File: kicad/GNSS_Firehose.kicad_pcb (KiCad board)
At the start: 4 copper layers, 117.9 x 99.1 mm, 460 parts, among them J1 SMA, J10 HEADER_16, J2 SMA, J3 SMA, J4 SMA, J5 SMA, J6 HEADER_14, J7 L829-1J1T-43, J8 PJ-063BH, Q1 Si2369DS, U1 MAX2112, U10 MAX19505, U11 AT25DF041A, U12 XC6SLX9-2TQG144C, U15 LMK03806, U17 LTC3633, U18 KSZ9031RNX, U19 CDCLVC1102, U2 MAX19505, U20 MIC2090-1YM5, U21 MIC2090-1YM5, U22 MIC2090-1YM5, U3 MGA-68563, U4 MAX2112, U5 MAX19505, U6 MGA-68563, U7 MAX2112, U8 MAX19505, U9 MGA-68563, Y1 25 MHz

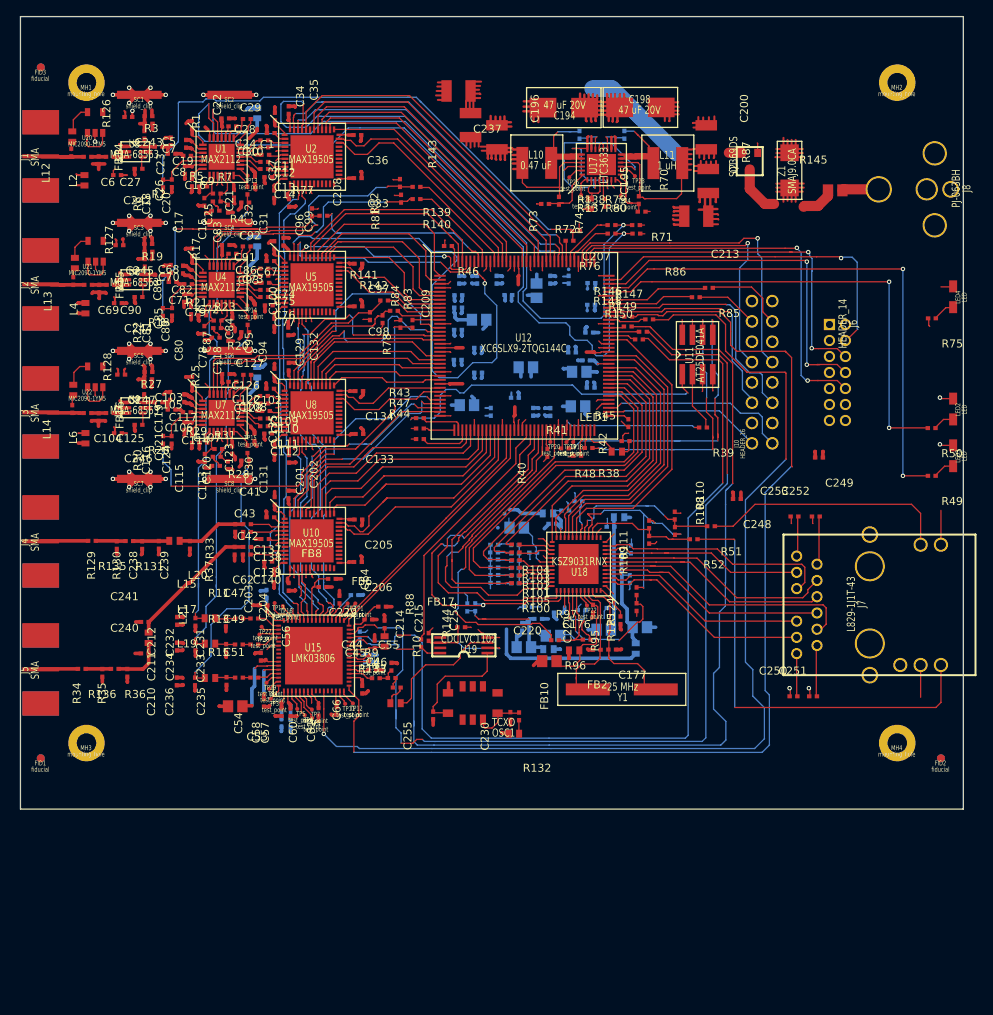
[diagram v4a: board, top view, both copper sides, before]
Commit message: add power-plane cutouts
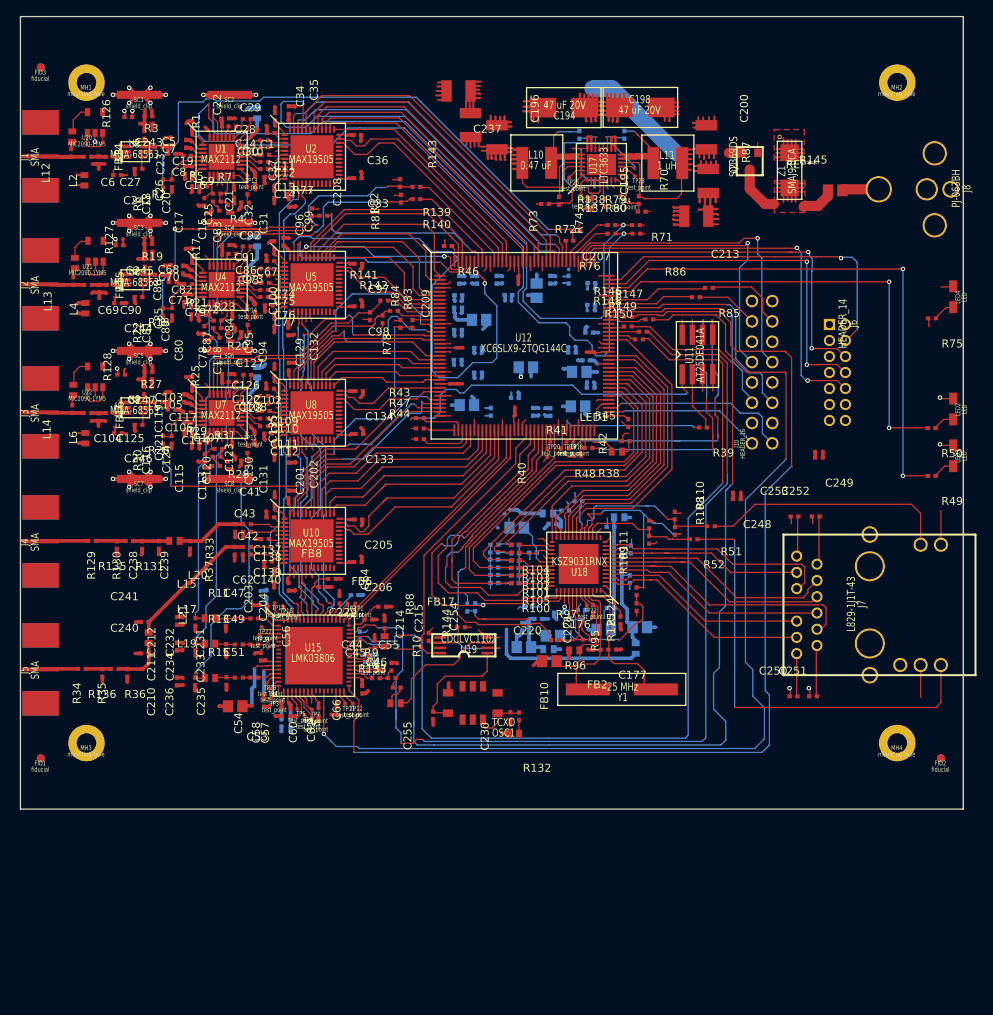
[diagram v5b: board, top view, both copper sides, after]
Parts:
- added REF**: via_12mil, footprints:via_12mil, F.Cu at (168.6, 58.2)
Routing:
- net VCC_1.2V: vias 0 -> 1
- net /RF channel 1/ch1_vcc_lna: vias 0 -> 1
- net /RF channel 1/ch1_vcc: vias 0 -> 1
- net /RF Channel 3/ch3_vcc_lna: vias 0 -> 1
- net /RF Channel 3/ch3_vcc: vias 0 -> 1
- net /RF Channel 2/ch2_vcc_lna: vias 0 -> 1
- net /RF Channel 2/ch2_vcc: vias 0 -> 1
- net /Ethernet/DVDDL: vias 0 -> 1
- net /Ethernet/DVDDH: vias 0 -> 1
- added copper zone on In2.Cu, net /Ethernet/DVDDH
- added copper zone on In2.Cu, net /Ethernet/DVDDL
- added copper zone on In2.Cu, net /RF Channel 2/ch2_vcc
- added copper zone on In2.Cu, net /RF Channel 2/ch2_vcc_lna
- added copper zone on In2.Cu, net /RF Channel 3/ch3_vcc
- added copper zone on In2.Cu, net /RF Channel 3/ch3_vcc_lna
- added copper zone on In2.Cu, net /RF channel 1/ch1_vcc
- added copper zone on In2.Cu, net /RF channel 1/ch1_vcc_lna
- added copper zone on F.Cu, net GND
- added copper zone on F.Cu, net Net-(Q1-Pad3)
- added copper zone on In2.Cu, net VCC_1.2V

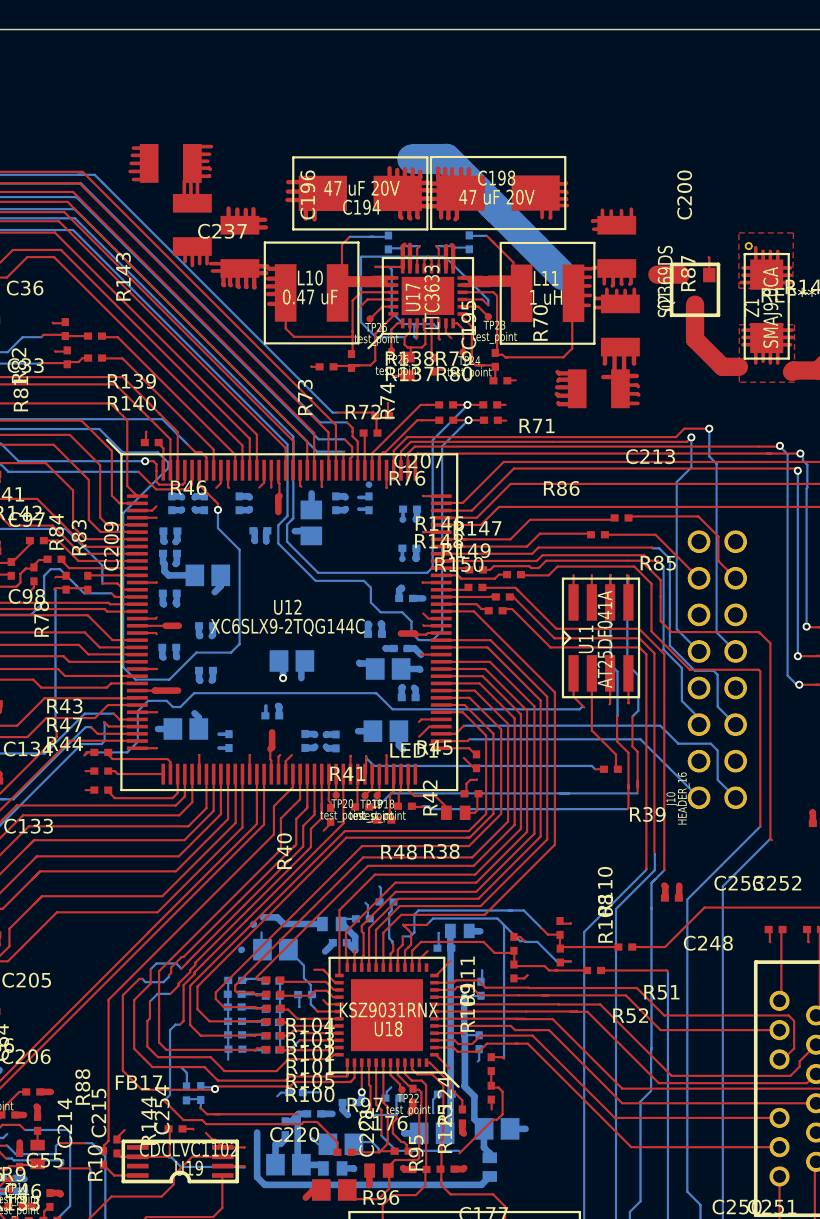
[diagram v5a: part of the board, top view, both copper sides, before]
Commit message: add small polygons
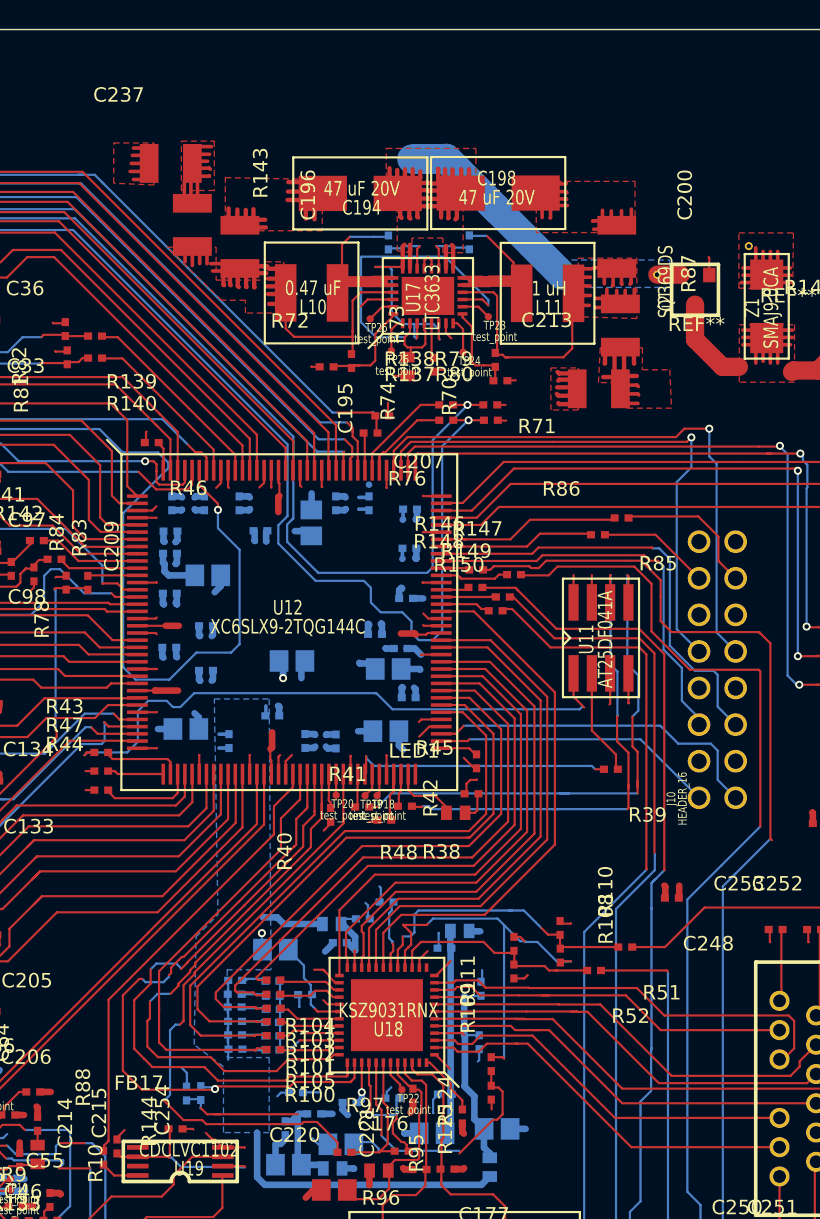
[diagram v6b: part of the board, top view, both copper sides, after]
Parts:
- added REF**: via_12mil, footprints:via_12mil, F.Cu at (162.2, 60.2)
- turned C182 to 180 degrees
- turned C183 to 180 degrees
- turned C193 to 180 degrees
- turned C195 to 270 degrees
- turned C197 to 270 degrees
- turned C213 to 180 degrees
- turned C223 to 180 degrees
- turned C237 to 180 degrees
- turned L10 to 180 degrees
- turned L11 to 180 degrees
- turned R143 to 90 degrees
- turned R70 to 270 degrees
- turned R72 to 180 degrees
- turned R73 to 90 degrees
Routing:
- net Net-(C199-Pad2): track 16.0 -> 25.1 mm
- net GND: track 430.9 -> 422.6 mm, vias 38 -> 39
- net Net-(C200-Pad1): track 30.9 -> 25.7 mm
- net (no net): track 1393.3 -> 1388.6 mm
- net Net-(R72-Pad1): track 4.64 -> 7.46 mm
- net /Ethernet/DVDDL: track 20.2 -> 22.9 mm
- net VCC_3.3V: track 161.6 -> 164.4 mm
- net /Ethernet/DVDDH: track 33.7 -> 36.0 mm
- net Net-(R70-Pad2): track 8.70 -> 6.44 mm
- net Net-(C197-Pad1): track 17.2 -> 15.1 mm
- net Net-(C197-Pad2): track 2.94 -> 3.81 mm
- added copper zone on B.Cu, net Net-(C194-Pad1)
- added copper zone on F.Cu, net Net-(C194-Pad1)
- added copper zone on F.Cu, net Net-(C196-Pad1)
- added copper zone on F.Cu, net Net-(C200-Pad1)
- added copper zone on B.Cu, net VCC_1.2V
- added copper zone on F.Cu, net VCC_1.2V
- added copper zone on F.Cu, net VCC_3.3V
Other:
- net class Default: clearance 0.15 -> 0.14986
- net class wide: clearance 0.15 -> 0.14986
- rule trace_clearance: 0.15 -> 0.14986

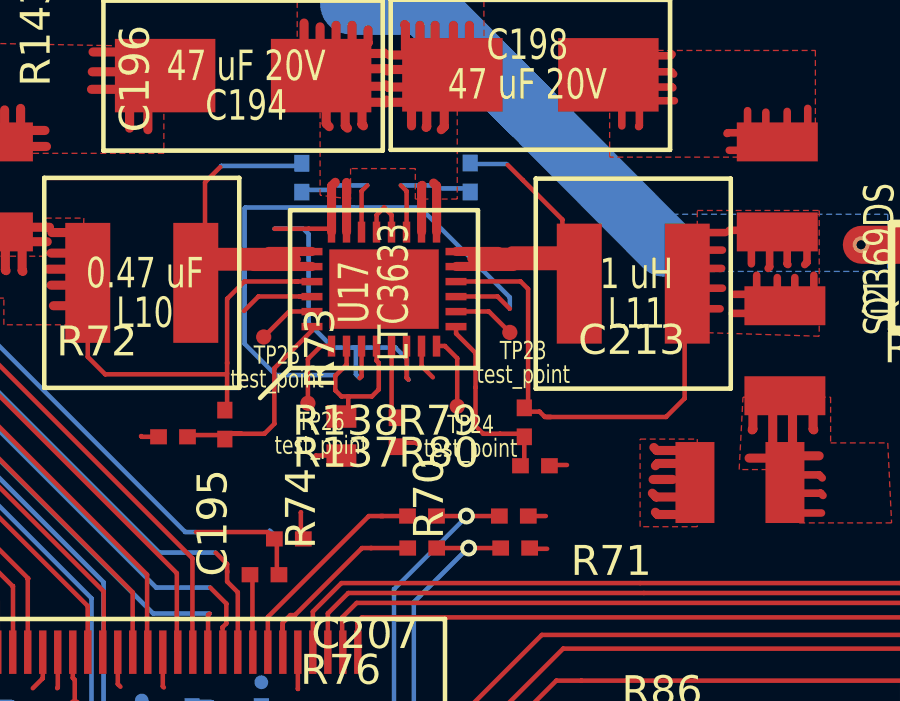
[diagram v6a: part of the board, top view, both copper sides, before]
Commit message: fix nearly all DRC errors
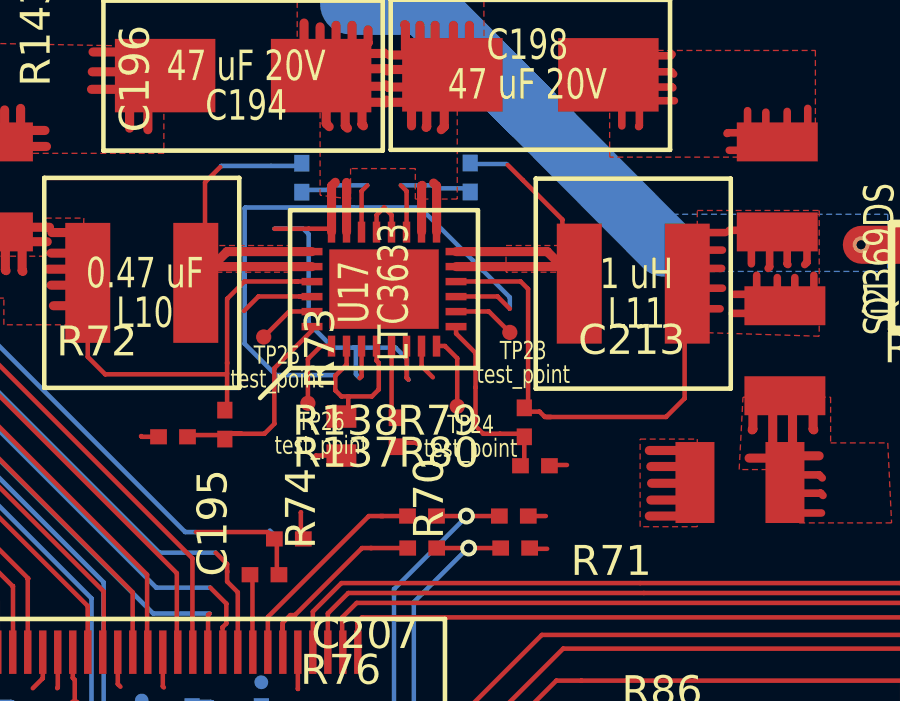
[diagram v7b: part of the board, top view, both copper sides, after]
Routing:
- net Net-(C199-Pad2): track 25.1 -> 16.2 mm
- net GND: track 422.6 -> 429.6 mm
- net (no net): track 1388.6 -> 1385.3 mm
- added copper zone on F.Cu, net Net-(C197-Pad1)
- added copper zone on F.Cu, net Net-(C199-Pad2)

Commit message: place vias
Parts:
- added G***: LOGO, footprints:diff-top, F.Cu at (132.6, 92.7)
- moved R126 0.21 mm to (80.3, 58.0)
- moved J2 0.06 mm to (73.2, 76.7)
- moved J3 0.06 mm to (73.2, 92.7)
- moved J4 0.06 mm to (73.1, 108.7)
- moved J1 0.06 mm to (73.2, 60.7)
- moved J5 0.06 mm to (73.2, 124.7)
- moved U21 0.06 mm to (82.1, 73.9)
- moved OSC1 0.06 mm to (134.0, 131.7)
- moved L12 0.05 mm to (80.0, 60.2)
- turned C53 to 180 degrees
- turned FB7 to 180 degrees
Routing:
- net (no net): track 1385.3 -> 200.2 mm
- net CLOCK_LE: track 32.6 -> 124.5 mm, vias 0 -> 3
- net CLOCK_DATA: track 29.9 -> 120.6 mm, vias 0 -> 3
- net CLOCK_FTEST_LD: track 47.4 -> 136.3 mm, vias 0 -> 1
- net CLOCK_CLK: track 28.7 -> 114.8 mm, vias 0 -> 3
- net CH1_GC1_FPGA_LPF: track 4.76 -> 71.0 mm, vias 0 -> 1
- net CH1_CLK+: track 3.72 -> 58.5 mm, vias 0 -> 2
- net CH1_REF+: track 3.99 -> 57.9 mm, vias 0 -> 2
- net CH1_CLK-: track 5.01 -> 58.6 mm, vias 0 -> 2
- net CH3_GC1_FPGA_LPF: track 3.01 -> 51.2 mm, vias 0 -> 4
- net CH1_SDIN: track 4.60 -> 52.1 mm, vias 0 -> 1
- net CH2_REF+: track 3.80 -> 44.0 mm, vias 0 -> 2
- net CH1_CS: track 5.72 -> 45.8 mm, vias 0 -> 1
- net CH1_SCLK: track 3.59 -> 43.2 mm, vias 0 -> 1
- net Net-(R43-Pad2): track 3.55 -> 42.2 mm, vias 0 -> 1
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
